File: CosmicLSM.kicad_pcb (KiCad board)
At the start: 4 copper layers, 44 x 44 mm, 50 parts, among them J1 BAT, J2 JST GH, J3 USB_C_Receptacle_USB2.0, SW1 SW_SPDT, SW2 SW_SPST, U1 SMF05CT1G, U2 SMF05CT1G, U3 M3406, U4 IP2312, U5 LSM6DSV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

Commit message: new data
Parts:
- removed G***: LOGO, CosmicLSM_Footprints:LunaFP
- removed R18: 5k1, CosmicLSM_Footprints:R_0603_1608Metric_Pad0.98x0.95mm_HandSolder
- removed U6: ESP32-C3-WROOM-02-N4, CosmicLSM_Footprints:MODULE_ESP32-C3-WROOM-02-H4
- added R22: 5k1, Resistor_SMD:R_0603_1608Metric_Pad0.98x0.95mm_HandSolder, F.Cu at (153.0, 85.0)
- added U7: ESP32-C6-MINI-1/U, Espressif:ESP32-C6-MINI-1, F.Cu at (147.5, 74.3)
- C1, C10, C11, C12, C2, C3, C4, C5, C6, C7, C8, C9: footprint CosmicLSM_Footprints:C_0603_1608Metric_Pad1.08x0.95mm_HandSolder -> Capacitor_SMD:C_0603_1608Metric_Pad1.08x0.95mm_HandSolder
- D1, D2, D3: footprint CosmicLSM_Footprints:LED_0603_1608Metric_Pad1.05x0.95mm_HandSolder -> LED_SMD:LED_0603_1608Metric_Pad1.05x0.95mm_HandSolder
- J1: footprint CosmicLSM_Footprints:JST_PH_S2B-PH-SM4-TB_1x02-1MP_P2.00mm_Horizontal -> Connector_JST:JST_PH_S2B-PH-SM4-TB_1x02-1MP_P2.00mm_Horizontal
- J2: footprint CosmicLSM_Footprints:JST_GH_SM05B-GHS-TB_1x05-1MP_P1.25mm_Horizontal -> Connector_JST:JST_GH_SM05B-GHS-TB_1x05-1MP_P1.25mm_Horizontal
- J3: footprint CosmicLSM_Footprints:USB_C_Receptacle_XKB_U262-16XN-4BVC11 -> Connector_USB:USB_C_Receptacle_XKB_U262-16XN-4BVC11
- L1: footprint CosmicLSM_Footprints:L_0603_1608Metric_Pad1.05x0.95mm_HandSolder -> Inductor_SMD:L_0603_1608Metric_Pad1.05x0.95mm_HandSolder
- L2: footprint CosmicLSM_Footprints:L_0805_2012Metric_Pad1.15x1.40mm_HandSolder -> Inductor_SMD:L_0805_2012Metric_Pad1.15x1.40mm_HandSolder
- R1, R10, R11, R12, R13, R14, R15, R16, R17, R19, R2, R20, R21, R3, R4, R5, R6, R7, R8, R9: footprint CosmicLSM_Footprints:R_0603_1608Metric_Pad0.98x0.95mm_HandSolder -> Resistor_SMD:R_0603_1608Metric_Pad0.98x0.95mm_HandSolder
- SW1: footprint CosmicLSM_Footprints:SW_SPDT_PCM12 -> Button_Switch_SMD:SW_SPDT_PCM12
- SW2: footprint CosmicLSM_Footprints:SW_SPST_B3U-1000P -> Button_Switch_SMD:SW_SPST_B3U-1000P
- U1, U2: footprint CosmicLSM_Footprints:SOT-363_SC-70-6 -> Package_TO_SOT_SMD:SOT-363_SC-70-6
- U3: footprint CosmicLSM_Footprints:SOT-23-5 -> Package_TO_SOT_SMD:SOT-23-5
- U4: footprint CosmicLSM_Footprints:HSOP-8-1EP_3.9x4.9mm_P1.27mm_EP2.41x3.1mm -> Package_SO:HSOP-8-1EP_3.9x4.9mm_P1.27mm_EP2.41x3.1mm
- U5: value LSM6DSV -> BMI160; footprint CosmicLSM_Footprints:Bosch_LGA-14_3x2.5mm_P0.5mm -> Package_LGA:Bosch_LGA-14_3x2.5mm_P0.5mm
- moved R19 22.8 mm to (157.0, 85.0), turned to 90 degrees
- moved R20 4.69 mm to (155.0, 85.0), turned to 90 degrees
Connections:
- U2 pad 5: USB_D- -> USB_D+
- U2 pad 6: USB_D+ -> USB_D-
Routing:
- net GND: track 106.6 -> 165.5 mm, vias 39 -> 46
- net USB_D+: track 44.5 -> 25.3 mm
- net USB_D-: track 44.0 -> 27.6 mm
- net ADC: track 13.0 -> 29.0 mm, vias 0 -> 2
- net STATUS_LED: track 43.9 -> 30.1 mm, vias 0 -> 2
- net +3V3: track 31.5 -> 42.7 mm, vias 12 -> 10
- net /BOOT: track 12.0 -> 22.6 mm, vias 2 -> 4
- net LSM_INT_MAIN: track 22.5 -> 13.2 mm
- net SDA: track 44.8 -> 52.1 mm
- net SCL: track 53.8 -> 49.6 mm, vias 5 -> 3
- net LSM_INT_AUX: track 44.6 -> 40.4 mm
- net /GPIO8: track 0.00 -> 4.17 mm
- net /EN: track 5.66 -> 9.36 mm
- net /GPIO2: track 3.20 -> 0.00 mm
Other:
- board text added: "BMI160"
- board text added: "Waifutracker v0.1"
- board text added: "Waifuwehr"
- board text added: "by Spacefish"
- board text removed: "Cosmic Slime v1"
- board text removed: "JLCJLCJLCJLC"
- board text removed: "LSM6DSV16X"
- board text removed: "by Higanbana"

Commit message: update to pcb
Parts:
- moved U7 0.78 mm to (147.5, 73.5)
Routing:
- net GND: track 165.5 -> 157.7 mm, vias 46 -> 45
- net USB_D-: track 27.6 -> 28.7 mm
- net USB_D+: track 25.3 -> 26.3 mm
- net LSM_INT_AUX: track 40.4 -> 41.5 mm
- net /BOOT: track 22.6 -> 23.4 mm
- net /GPIO8: track 4.17 -> 4.94 mm
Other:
- outline, holes or cut-outs redrawn

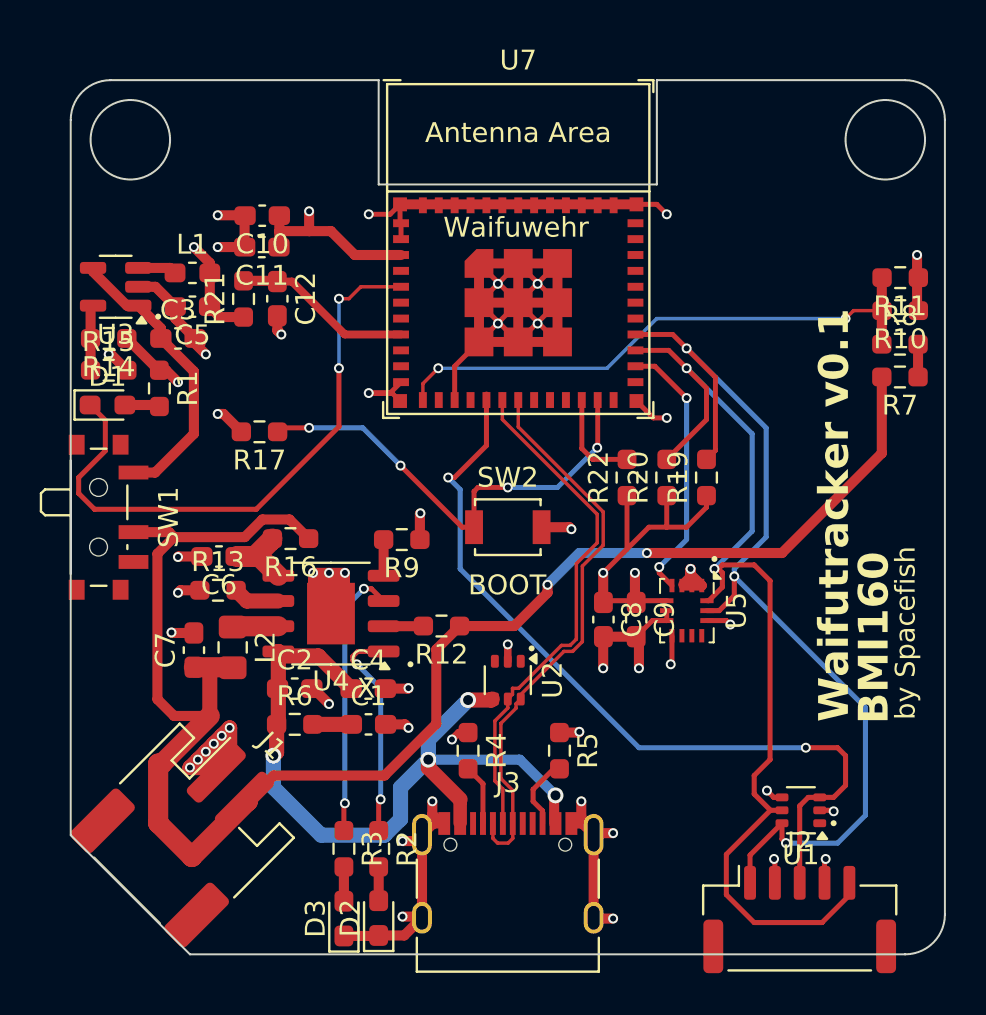
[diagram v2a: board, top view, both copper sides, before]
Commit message: remove backup files
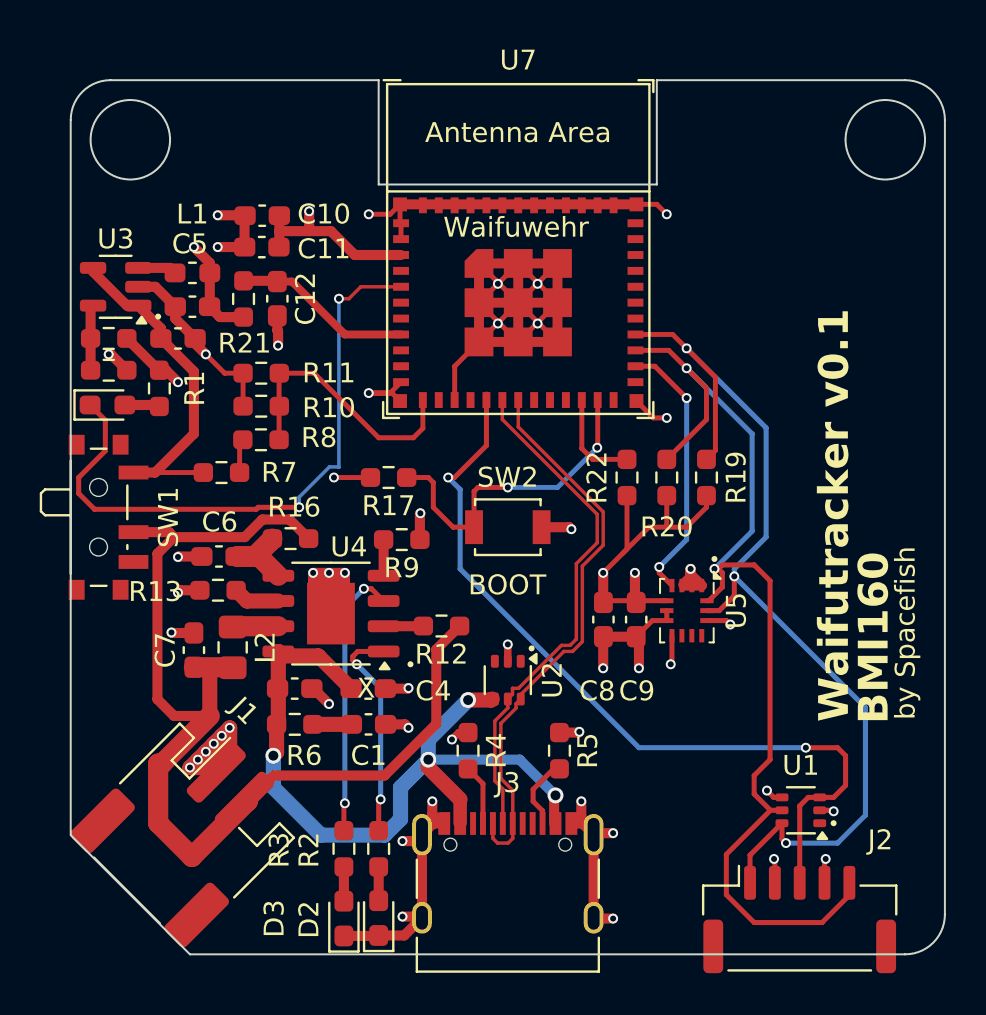
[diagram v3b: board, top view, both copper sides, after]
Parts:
- moved R7 34.5 mm to (132.6, 84.8)
- moved R8 32.5 mm to (134.6, 83.1), turned to 180 degrees
- moved R10 32.5 mm to (134.6, 81.4), turned to 0 degrees
- moved R11 32.5 mm to (134.6, 79.8), turned to 0 degrees
- moved R17 6.89 mm to (141.0, 85.0)
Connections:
- R7 pad 2: +BATT -> VCC
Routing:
- net +BATT: track 85.9 -> 57.0 mm, vias 2 -> 0
- net ADC: track 28.5 -> 13.6 mm, vias 2 -> 0
- net /BOOT: track 23.4 -> 16.5 mm, vias 4 -> 2
- net VCC: track 14.6 -> 18.1 mm
- net GND: track 157.7 -> 159.3 mm, vias 45 -> 44
- net STATUS_LED: track 30.3 -> 31.8 mm

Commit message: inductors
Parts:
- J3: value USB_C_Receptacle_USB2.0 -> ~; footprint Connector_USB:USB_C_Receptacle_XKB_U262-16XN-4BVC11 -> usb_c_connector:USB-C-SMD_G-SWITCH_GT-USB-7010ASV
- L1: footprint Inductor_SMD:L_0603_1608Metric_Pad1.05x0.95mm_HandSolder -> 3_3v_coil:IND-SMD_L2.0-W1.6_GCDA201610P-R24MC
- L2: footprint Inductor_SMD:L_0805_2012Metric_Pad1.15x1.40mm_HandSolder -> Inductor_SMD:L_1008_2520Metric_Pad1.43x2.20mm_HandSolder
- SW1: value SW_SPDT -> ~; footprint Button_Switch_SMD:SW_SPDT_PCM12 -> Data:SW-SMD_MK-11C04-G013
- SW2: value SW_SPST -> ~; footprint Button_Switch_SMD:SW_SPST_B3U-1000P -> boot_button:SW-SMD_4P-L5.1-W5.1-P3.70-LS6.5-TL-2
- moved SW2 1.58 mm to (147.9, 88.8), turned to 90 degrees
- moved J3 1.21 mm to (147.0, 104.9)
- moved C7 1.00 mm to (130.2, 94.0)
- moved L1 0.57 mm to (130.8, 74.2)
- moved L2 0.45 mm to (132.8, 93.8)
- moved SW1 0.15 mm to (126.9, 87.0)
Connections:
- SW1 pad 2: +BATT -> unconnected-(SW1-Pad2)
- SW2 pad 1: /BOOT -> unconnected-(SW2-A-Pad1)
- SW2 pad 2: GND -> /BOOT
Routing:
- net STATUS_LED: track 31.8 -> 20.0 mm
- net /BOOT: track 16.5 -> 14.3 mm
- net GND: track 159.3 -> 160.9 mm, vias 44 -> 45
- net +BATT: track 57.0 -> 55.6 mm
- net +3V3: track 42.7 -> 42.4 mm, vias 10 -> 12

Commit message: ordered
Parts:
- J3: value ~ -> USB-C
- SW1: value ~ -> PWR SW
- SW2: value ~ -> BOOT BTN
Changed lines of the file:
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@@
 		(sheetname "Root")
 		(sheetfile "CosmicLSM.kicad_sch")
-		(attr smd)
+		(attr smd dnp)
 		(fp_line
 			(start -4.86 -1.71)
@@
 			)
 		)
-		(property "Value" "~"
+		(property "Value" "USB-C"
 			(at 0 5.857 0)
 			(unlocked yes)
@@
 		(tags "inductor handsolder")
 		(property "Reference" "L2"
-			(at 0 -2.05 -90)
+			(at 1.25 4.25 -90)
 			(layer "F.SilkS")
 			(effects
@@
 		(tags "capacitor handsolder")
 		(property "Reference" "C7"
-			(at -0.3125 -3.2 90)
+			(at -1 -3.25 90)
 			(layer "F.SilkS")
 			(effects
@@
 			)
 		)
-		(property "Value" "~"
+		(property "Value" "BOOT BTN"
 			(at 0 3.377 90)
 			(unlocked yes)
@@
 			)
 		)
-		(property "Value" "~"
+		(property "Value" "PWR SW"
 			(at 0 4.007 -90)
 			(unlocked yes)
